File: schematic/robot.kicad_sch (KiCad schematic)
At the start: 28 parts, among them M1 MOTOR, M2 MOTOR, M3 MOTOR, M4 MOTOR, M5 MOTOR, M6 SERVO, M7 SERVO, U10 HALL-EFFECT, U12 MEEN3230_POWER_BOARD, U4 ENCODER, U5 ENCODER, U6 ENCODER, U7 BUCKCONVERTER, U8 SHARPDISTANCE, U9 TCS3200

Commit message: Full PM7 working
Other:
- note added: "Note to self, flip M1 and M3"
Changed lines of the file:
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@@
+		)
+	)
+	(text "Note to self, flip M1 and M3"
+		(exclude_from_sim no)
+		(at 136.652 87.376 0)
+		(effects
+			(font
+				(size 1.27 1.27)
+			)
 		)
 	)

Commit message: I don't even know at this point, so much changed
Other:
- sheet Motors ports: added MC1_1, MC1_2, MC1_3, MC1_4, MC1_5, MC1_6, MC2_1, MC2_2, MC2_3, MC2_4, MC2_5, MC2_6, MC3_1, MC3_2, MC3_3, MC3_4, MC3_5, MC3_6; removed MC1, MC10, MC11, MC12, MC13, MC14, MC15, MC16, MC17, MC18, MC2, MC3, MC4, MC5, MC6, MC7, MC8, MC9
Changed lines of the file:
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@@
-			)
-		)
-		(pin "MC1" input
-			(at 143.51 38.1 180)
-			(effects
-				(font
-					(size 1.27 1.27)
-				)
-				(justify left)
-			)
-		)
-		(pin "MC2" input
-			(at 143.51 40.64 180)
-			(effects
-				(font
-					(size 1.27 1.27)
-				)
-				(justify left)
-			)
-		)
-		(pin "MC3" input
-			(at 143.51 43.18 180)
-			(effects
-				(font
-					(size 1.27 1.27)
-				)
-				(justify left)
-			)
-		)
-		(pin "MC4" input
-			(at 143.51 45.72 180)
-			(effects
-				(font
-					(size 1.27 1.27)
-				)
-				(justify left)
-			)
-		)
-		(pin "MC5" input
-			(at 143.51 48.26 180)
-			(effects
-				(font
-					(size 1.27 1.27)
-				)
-				(justify left)
-			)
-		)
-		(pin "MC6" input
-			(at 143.51 50.8 180)
-			(effects
-				(font
-					(size 1.27 1.27)
-				)
-				(justify left)
-			)
-		)
-		(pin "MC7" input
-			(at 143.51 53.34 180)
-			(effects
-				(font
-					(size 1.27 1.27)
-				)
-				(justify left)
-			)
-		)
-		(pin "MC8" input
-			(at 143.51 55.88 180)
-			(effects
-				(font
-					(size 1.27 1.27)
-				)
-				(justify left)
-			)
-		)
-		(pin "MC9" input
-			(at 143.51 58.42 180)
-			(effects
-				(font
-					(size 1.27 1.27)
-				)
-				(justify left)
-			)
-		)
-		(pin "MC10" input
-			(at 143.51 60.96 180)
-			(effects
-				(font
-					(size 1.27 1.27)
-				)
-				(justify left)
-			)
-		)
-		(pin "MC11" input
-			(at 143.51 63.5 180)
-			(effects
-				(font
-					(size 1.27 1.27)
-				)
-				(justify left)
-			)
-		)
-		(pin "MC12" input
-			(at 143.51 66.04 180)
-			(effects
-				(font
-					(size 1.27 1.27)
-				)
-				(justify left)
-			)
-		)
-		(pin "MC13" input
-			(at 143.51 68.58 180)
-			(effects
-				(font
-					(size 1.27 1.27)
-				)
-				(justify left)
-			)
-		)
-		(pin "MC14" input
-			(at 143.51 71.12 180)
-			(effects
-				(font
-					(size 1.27 1.27)
-				)
-				(justify left)
-			)
-		)
-		(pin "MC15" input
-			(at 143.51 73.66 180)
-			(effects
-				(font
-					(size 1.27 1.27)
-				)
-				(justify left)
-			)
-		)
-		(pin "MC16" input
-			(at 143.51 76.2 180)
-			(effects
-				(font
-					(size 1.27 1.27)
-				)
-				(justify left)
-			)
-		)
-		(pin "MC17" input
-			(at 143.51 78.74 180)
-			(effects
-				(font
-					(size 1.27 1.27)
-				)
-				(justify left)
-			)
-		)
-		(pin "MC18" input
-			(at 143.51 81.28 180)
-			(effects
-				(font
-					(size 1.27 1.27)
-				)
-				(justify left)
 			)
 		)
@@
 			)
 		)
+		(pin "MC1_1" input
+			(at 143.51 38.1 180)
+			(effects
+				(font
+					(size 1.27 1.27)
+				)
+				(justify left)
+			)
+		)
+		(pin "MC1_2" input
+			(at 143.51 40.64 180)
+			(effects
+				(font
+					(size 1.27 1.27)
+				)
+				(justify left)
+			)
+		)
+		(pin "MC1_3" input
+			(at 143.51 43.18 180)
+			(effects
+				(font
+					(size 1.27 1.27)
+				)
+				(justify left)
+			)
+		)
+		(pin "MC1_4" input
+			(at 143.51 45.72 180)
+			(effects
+				(font
+					(size 1.27 1.27)
+				)
+				(justify left)
+			)
+		)
+		(pin "MC1_5" input
+			(at 143.51 48.26 180)
+			(effects
+				(font
+					(size 1.27 1.27)
+				)
+				(justify left)
+			)
+		)
+		(pin "MC1_6" input
+			(at 143.51 50.8 180)
+			(effects
+				(font
+					(size 1.27 1.27)
+				)
+				(justify left)
+			)
+		)
+		(pin "MC2_1" input
+			(at 143.51 53.34 180)
+			(effects
+				(font
+					(size 1.27 1.27)
+				)
+				(justify left)
+			)
+		)
+		(pin "MC2_2" input
+			(at 143.51 55.88 180)
+			(effects
+				(font
+					(size 1.27 1.27)
+				)
+				(justify left)
+			)
+		)
+		(pin "MC2_3" input
+			(at 143.51 58.42 180)
+			(effects
+				(font
+					(size 1.27 1.27)
+				)
+				(justify left)
+			)
+		)
+		(pin "MC2_4" input
+			(at 143.51 60.96 180)
+			(effects
+				(font
+					(size 1.27 1.27)
+				)
+				(justify left)
+			)
+		)
+		(pin "MC2_5" input
+			(at 143.51 63.5 180)
+			(effects
+				(font
+					(size 1.27 1.27)
+				)
+				(justify left)
+			)
+		)
+		(pin "MC2_6" input
+			(at 143.51 66.04 180)
+			(effects
+				(font
+					(size 1.27 1.27)
+				)
+				(justify left)
+			)
+		)
+		(pin "MC3_1" input
+			(at 143.51 68.58 180)
+			(effects
+				(font
+					(size 1.27 1.27)
+				)
+				(justify left)
+			)
+		)
+		(pin "MC3_2" input
+			(at 143.51 71.12 180)
+			(effects
+				(font
+					(size 1.27 1.27)
+				)
+				(justify left)
+			)
+		)
+		(pin "MC3_3" input
+			(at 143.51 73.66 180)
+			(effects
+				(font
+					(size 1.27 1.27)
+				)
+				(justify left)
+			)
+		)
+		(pin "MC3_4" input
+			(at 143.51 76.2 180)
+			(effects
+				(font
+					(size 1.27 1.27)
+				)
+				(justify left)
+			)
+		)
+		(pin "MC3_5" input
+			(at 143.51 78.74 180)
+			(effects
+				(font
+					(size 1.27 1.27)
+				)
+				(justify left)
+			)
+		)
+		(pin "MC3_6" input
+			(at 143.51 81.28 180)
+			(effects
+				(font
+					(size 1.27 1.27)
+				)
+				(justify left)
+			)
+		)

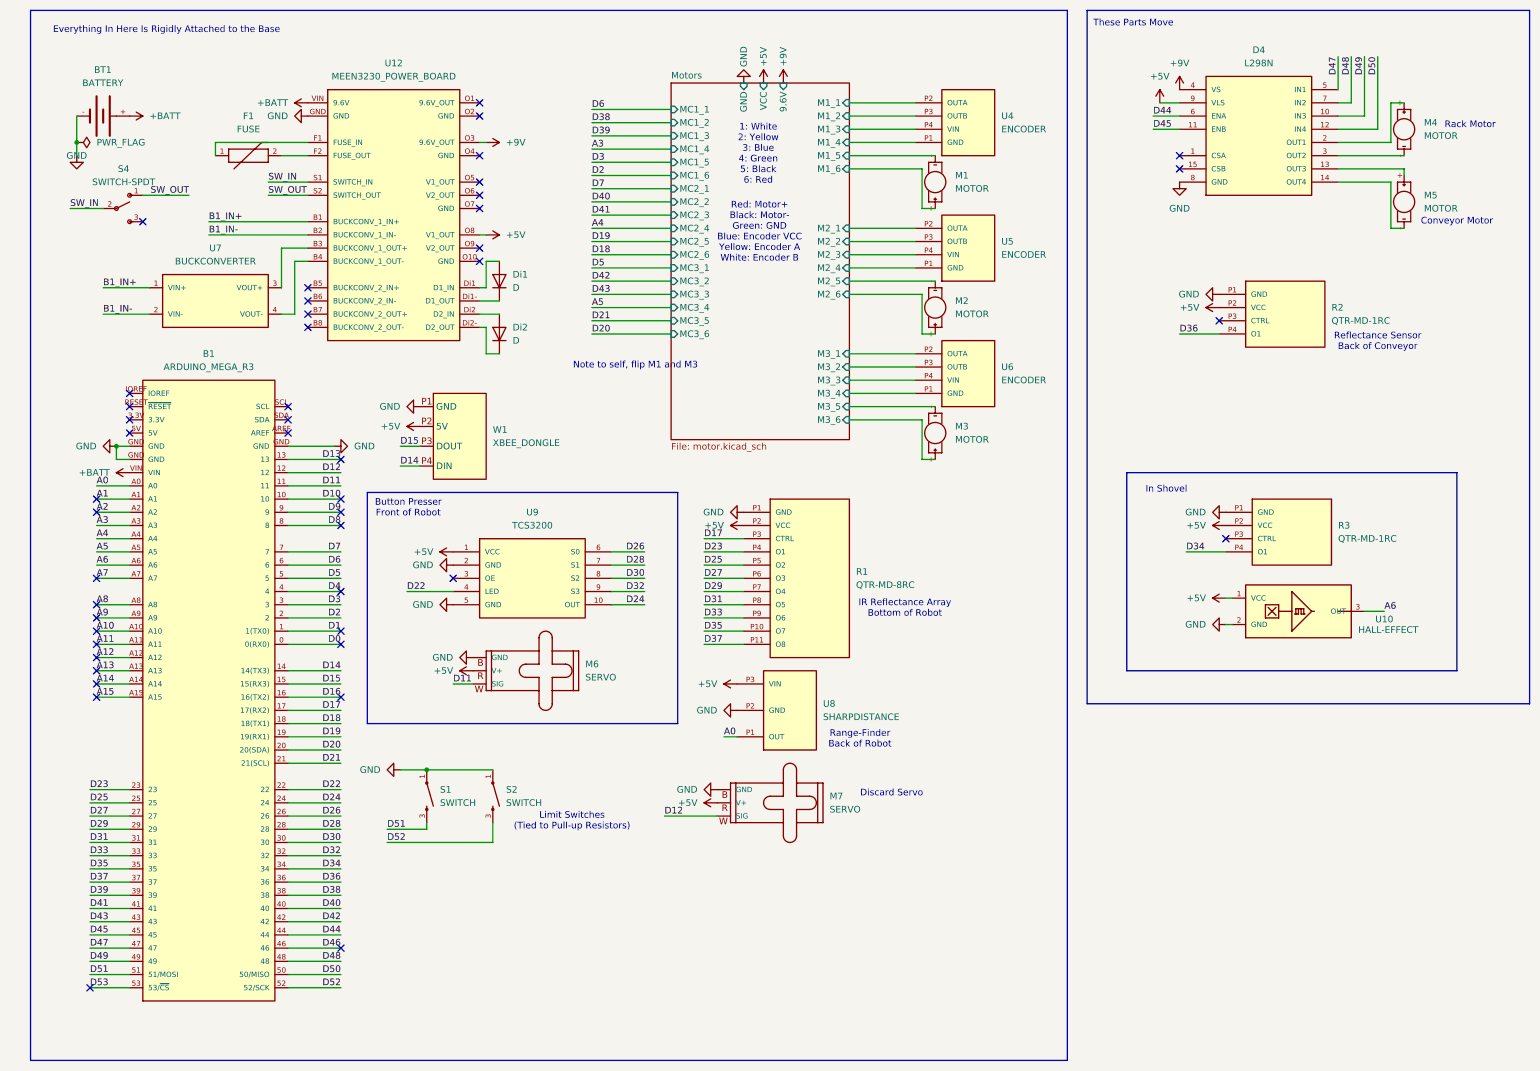
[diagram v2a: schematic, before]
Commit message: Added second rangefinder to schematic
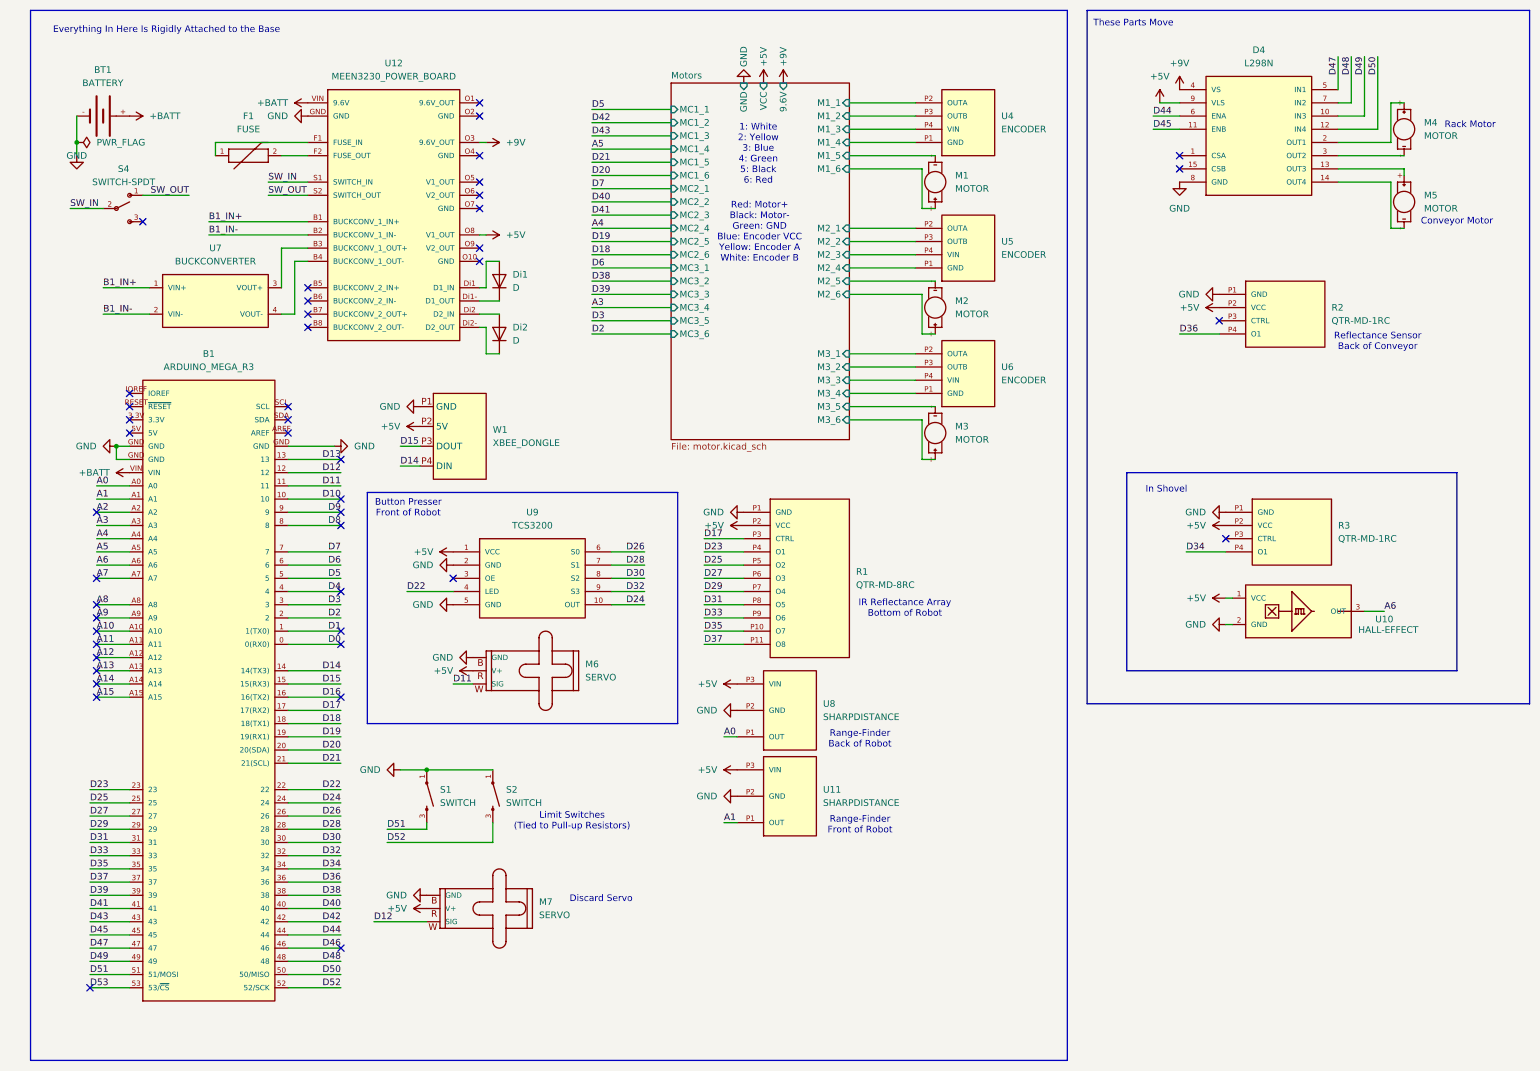
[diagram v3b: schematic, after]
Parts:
- added U11: SHARPDISTANCE, SHARPDISTANCE:SHARPDISTANCE, symbol ME3230:SHARPDISTANCE
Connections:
- net +5V: now also U11.P3 (VIN)
- net A1: now also U11.P1 (OUT)
- net GND: now also U11.P2 (GND)
- no-connect marks 46 -> 45
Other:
- note added: "Range-Finder Front of Robot"
- note removed: "Note to self, flip M1 and M3"
- moved on the sheet: M7

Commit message: moved servo pins because PWMServo is jank AF
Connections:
- net D11: now also D4.6 (ENA); no longer M6. (V+)
- net D12: now also D4.11 (ENB); no longer M7. (V+)
- net D44: now also M6. (V+); no longer D4.6 (ENA)
- net D45: now also M7. (V+); no longer D4.11 (ENB)
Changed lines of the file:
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@@
 		)
 	)
-	(label "D45"
+	(label "D12"
 		(at 236.22 41.91 0)
 		(effects
@@
 		)
 	)
-	(label "D11"
+	(label "D44"
 		(at 101.6 148.59 0)
 		(effects
@@
 		)
 	)
-	(label "D12"
+	(label "D45"
 		(at 86.36 194.31 0)
 		(effects
@@
 		)
 	)
-	(label "D44"
+	(label "D11"
 		(at 236.22 39.37 0)
 		(effects

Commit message: new
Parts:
- added C1, C2: 100nF, CAPACITOR:CAPACITOR, symbol ME3230:CAPACITOR
- added R4, R5: ~, RESISTOR:RESISTORFOOTPRINT, symbol ME3230:RESISTOR
- added R6: 47k, RESISTOR:RESISTORFOOTPRINT, symbol ME3230:RESISTOR
- added R7: 2k, RESISTOR:RESISTORFOOTPRINT, symbol ME3230:RESISTOR
- added RV1: POT, POT:TRIM_POT, symbol ME3230:POT
- added U13: MCP6004, symbol Amplifier_Operational:MCP6004
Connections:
- net +5V: now also C2.1, R5.
- net A6: now also C1.2, R6., U13.1; no longer U10.3 (OUT)
- net D11: now also M6. (V+); no longer D4.6 (ENA)
- net D12: now also M7. (V+); no longer D4.11 (ENB)
- net D17: no longer R1.P3 (CTRL)
- net D44: now also D4.6 (ENA); no longer M6. (V+)
- net D45: now also D4.11 (ENB); no longer M7. (V+)
- net GND: now also U10.3 (OUT), C2.2, R4.; no longer U10.2 (GND)
- new net: R4., RV1.3
- new net: RV1.1, U13.2 (-)
- new net: R5., RV1.2
- new net: C1.1, R6., R7., U13.3 (+)
- new net H3: R7., U10.2 (GND)
- no-connect marks 45 -> 47
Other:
- note added: "Hall-Effect Filter"
- moved on the sheet: U10

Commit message: PM8?
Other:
- note added: "Black White Grey Purple"
- note added: "Blue"
- note added: "Green"
- note added: "Orange"
- note added: "Yellow"
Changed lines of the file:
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@@
+		)
+	)
+	(text "Yellow"
+		(exclude_from_sim no)
+		(at 89.154 130.81 0)
+		(effects
+			(font
+				(size 1.27 1.27)
+			)
 		)
 	)
@@
 		)
 	)
+	(text "Black\nWhite\nGrey\nPurple"
+		(exclude_from_sim no)
+		(at 141.478 126.492 0)
+		(effects
+			(font
+				(size 1.397 1.397)
+			)
+		)
+	)
+	(text "Green"
+		(exclude_from_sim no)
+		(at 90.17 123.19 0)
+		(effects
+			(font
+				(size 1.27 1.27)
+			)
+		)
+	)
 	(text "Conveyor Motor"
 		(exclude_from_sim no)
 		(at 294.64 59.69 0)
+		(effects
+			(font
+				(size 1.27 1.27)
+			)
+		)
+	)
+	(text "Orange"
+		(exclude_from_sim no)
+		(at 90.17 133.35 0)
 		(effects
 			(font
@@
 		(effects
 			(font
+				(size 1.27 1.27)
+			)
+		)
+	)
+	(text "Blue"
+		(exclude_from_sim no)
+		(at 140.97 133.35 0)
+		(effects
+			(font

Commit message: updated schematic
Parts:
- added M8: SERVO, SERVO:SERVOFOOTPRINT, symbol ME3230:SERVO
- R4, R5: value ~ -> (none)
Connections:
- net +5V: now also M8. (V+)
- net D11: now also M8. (V+); no longer M6. (V+)
- net D13: now also M6. (V+)
- net GND: now also M8. (V+)
- no-connect marks 47 -> 46
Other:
- note added: "Reflectance Sensor Back of Gate"
- note removed: "Reflectance Sensor Back of Conveyor"
- moved on the sheet: R3

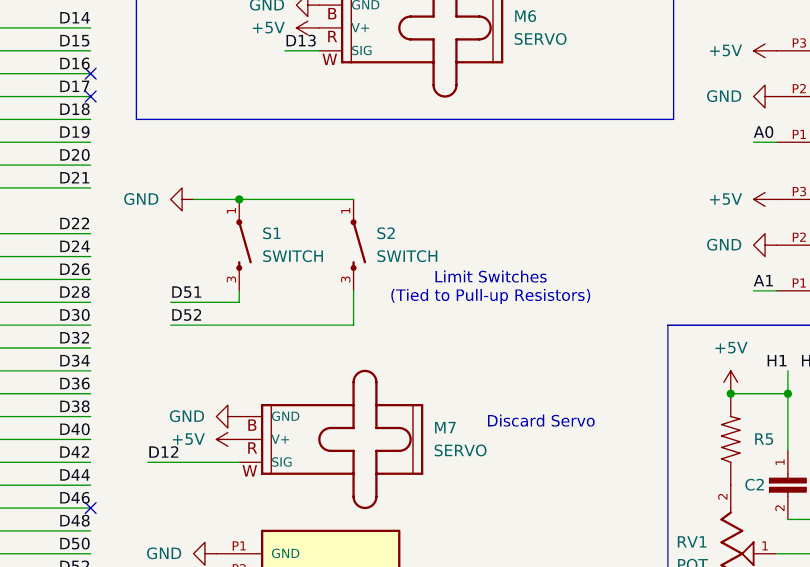
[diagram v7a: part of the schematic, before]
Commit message: added shovel switch
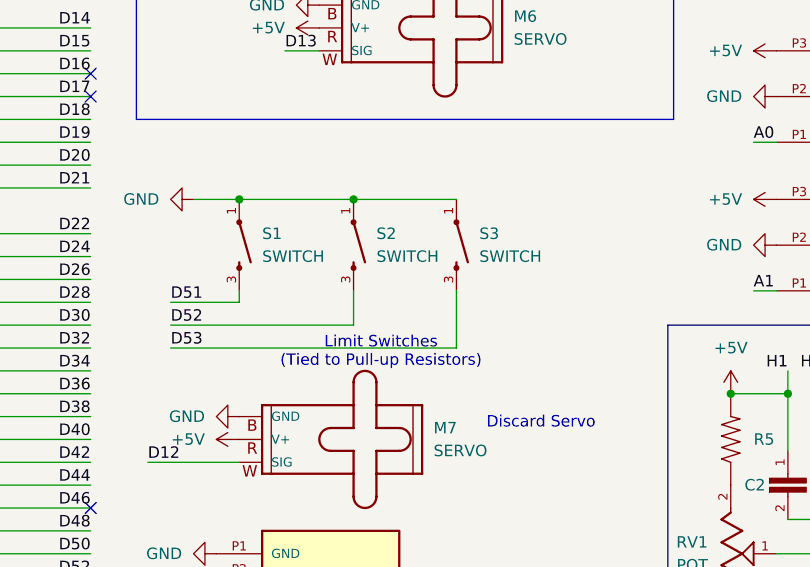
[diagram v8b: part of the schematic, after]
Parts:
- added S3: SWITCH, MechLibrary:Header3, symbol ME3230:PUSHBUTTON-SWITCH
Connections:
- net D53: now also S3.3
- net GND: now also S3.1
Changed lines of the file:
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@@
 	(text "Limit Switches\n(Tied to Pull-up Resistors)"
 		(exclude_from_sim no)
-		(at 124.46 175.006 0)
+		(at 112.268 182.118 0)
 		(effects
 			(font
@@
 	)
 	(junction
+		(at 109.22 165.1)
+		(diameter 0)
+		(color 0 0 0 0)
+	)
+	(junction
 		(at 161.29 212.09)
 		(diameter 0)
@@
 	(wire
 		(pts
+			(xy 88.9 181.61) (xy 120.65 181.61)
+		)
+		(stroke
+			(width 0)
+			(type default)
+		)
+	)
+	(wire
+		(pts
 			(xy 157.48 184.15) (xy 157.48 186.69)
 		)
@@
 	(wire
 		(pts
+			(xy 120.65 175.26) (xy 120.65 181.61)
+		)
+		(stroke
+			(width 0)
+			(type default)
+		)
+	)
+	(wire
+		(pts
+			(xy 109.22 165.1) (xy 120.65 165.1)
+		)
+		(stroke
+			(width 0)
+			(type default)
+		)
+	)
+	(wire
+		(pts
 			(xy 281.94 60.96) (xy 284.48 60.96)
 		)
@@
 		)
 	)
+	(label "D53"
+		(at 88.9 181.61 0)
+		(effects
+			(font
+				(size 1.27 1.27)
+			)
+			(justify left bottom)
+		)
+	)
 	(label "D51"
 		(at 88.9 176.53 0)
@@
 					(unit 1)
 				)
+			)
+		)
+	)
+	(symbol
+		(lib_id "ME3230:PUSHBUTTON-SWITCH")
+		(at 120.65 170.18 270)
+		(unit 1)
+		(body_style 1)
+		(exclude_from_sim no)
+		(in_bom yes)
+		(on_board yes)
+		(in_pos_files yes)
+		(dnp no)
+		(fields_autoplaced yes)
+		(property "Reference" "S3"
+			(at 123.19 168.9099 90)
+			(show_name no)
+			(do_not_autoplace no)
+			(effects
+				(font
+					(size 1.27 1.27)
+				)
+				(justify left)
+			)
+		)
+		(property "Value" "SWITCH"
+			(at 123.19 171.4499 90)
+			(show_name no)
+			(do_not_autoplace no)
+			(effects
+				(font
+					(size 1.27 1.27)
+				)
+				(justify left)
+			)
+		)
+		(property "Footprint" "MechLibrary:Header3"
+			(at 115.824 170.18 0)
+			(hide yes)
+			(show_name no)
+			(do_not_autoplace no)
+			(effects
+				(font
+					(size 1.27 1.27)
+				)
+				(justify bottom)
+			)
+		)
+		(property "Datasheet" ""
+			(at 120.65 170.18 0)
+			(hide yes)
+			(show_name no)
+			(do_not_autoplace no)
+			(effects
+				(font
+					(size 1.27 1.27)
+				)
+			)
+		)
+		(property "Description" ""
+			(at 120.65 170.18 0)
+			(hide yes)
+			(show_name no)
+			(do_not_autoplace no)
+			(effects
+				(font
+					(size 1.27 1.27)
+				)
+			)
+		)
+		(pin "3"
+		)
+		(pin "1"
+		)
+		(instances
+			(project "robot"
+				(path "/c33baf39-1524-47fd-8733-9db21030ba51"
+					(reference "S3")
+					(unit 1)
+				)
